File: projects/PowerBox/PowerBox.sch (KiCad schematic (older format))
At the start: 39 parts

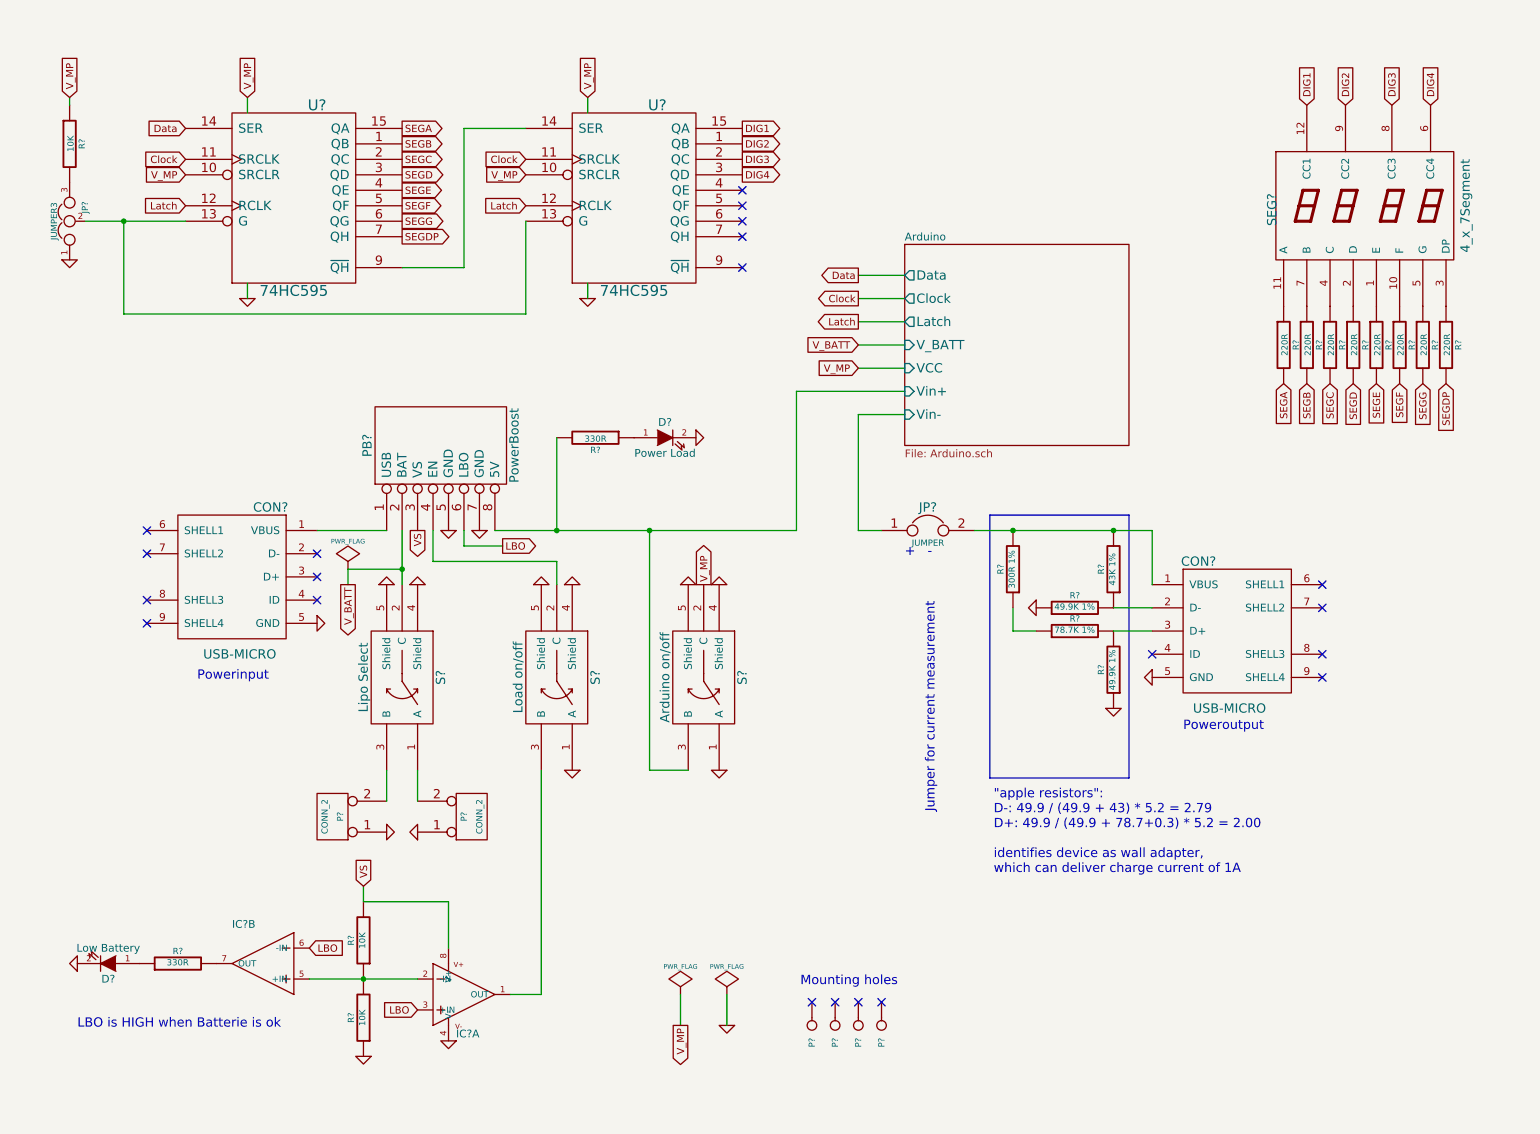
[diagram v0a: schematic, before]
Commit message: erc warnings solved
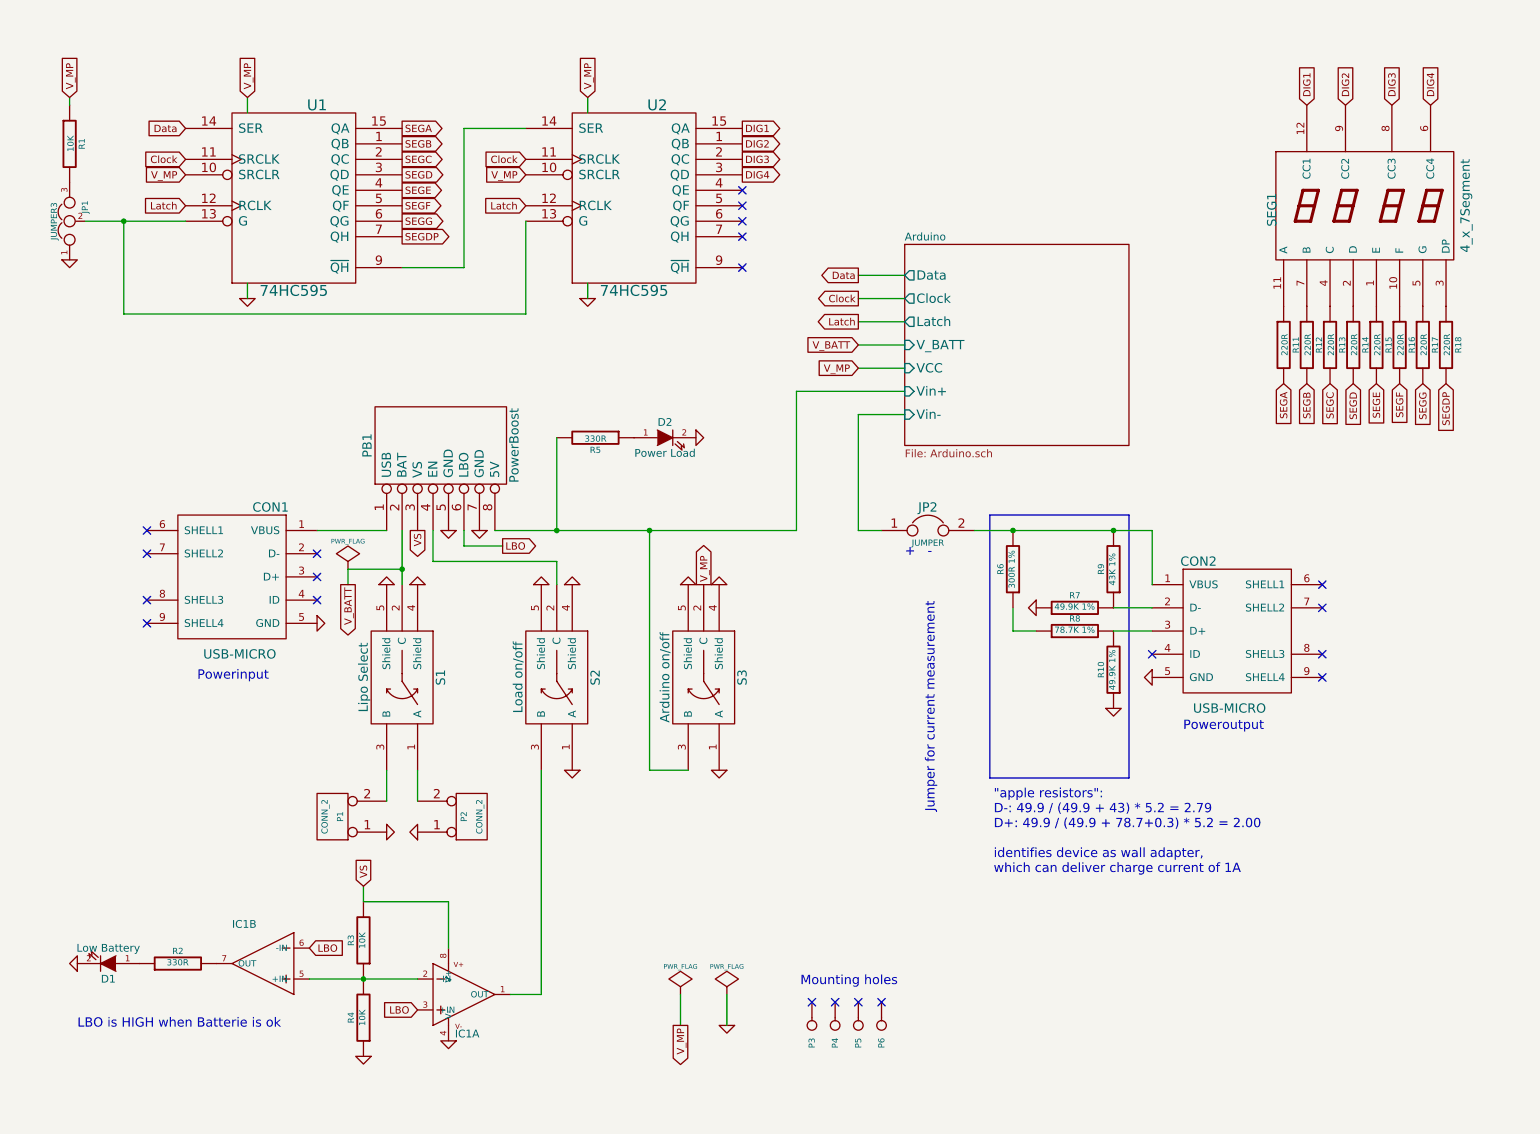
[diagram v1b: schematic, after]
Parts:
- gave numbers to parts that had none: 38

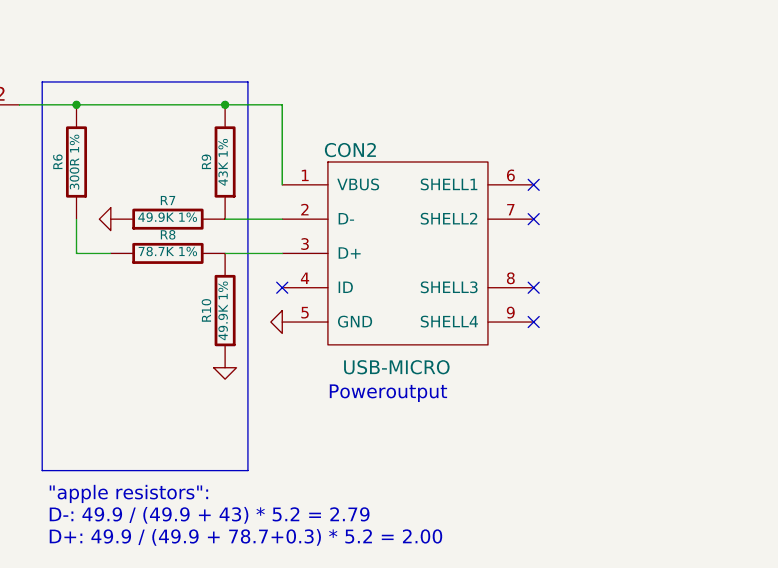
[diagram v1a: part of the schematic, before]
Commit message: more footprints added
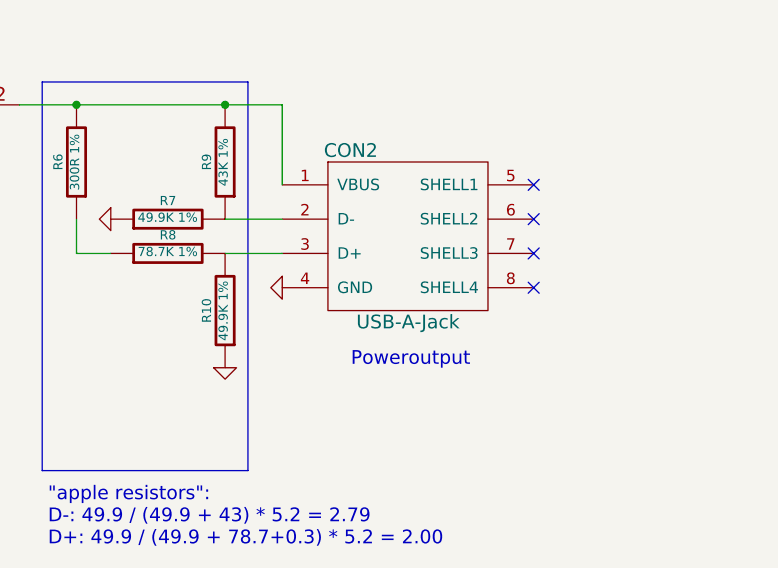
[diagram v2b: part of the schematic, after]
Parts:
- removed CON2: USB-MICRO, symbol USB-MICRO
- added CON2: USB-A-Jack, frep:USB-A-Jack, symbol USB-A-Jack
- CON1: footprint (none) -> frep:USB_Micro
- D1, D2: footprint (none) -> frep:LED-0805
- IC1: footprint SparkFun-SO08 -> frep:SOIC8
- JP1: footprint (none) -> frep:Pin_Proto_Straight_1x03
- JP2: footprint (none) -> frep:Pin_Proto_Straight_1x02
- P1: footprint (none) -> frep:JST-PH-2-THM
- P2: footprint (none) -> frep:JST-PH-2-THM-RA
- P3, P4, P5, P6: footprint (none) -> frep:MountingHole_3mm
- PB1: footprint (none) -> frep:Powerboost1000C
- R1, R10, R11, R12, R13, R14, R15, R16, R17, R18, R2, R3, R4, R5, R6, R7, R8, R9: footprint (none) -> frep:R0805
- S1, S2, S3: footprint (none) -> frep:Switch_SPDT
- SEG1: footprint (none) -> frep:4digit7segment
- U1, U2: footprint (none) -> frep:SO16
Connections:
- net GND: now also CON2.4 (GND)
- net at JP2.2, R6.2, R9.2: now also CON2.1 (VBUS)
- net at R7.2, R9.1: now also CON2.2 (D-)
- net at R10.2, R8.2: now also CON2.3 (D+)
- no-connect marks 21 -> 20
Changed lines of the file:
@@
 LIBS:frep
 LIBS:PowerBox-cache
-EELAYER 24 0
+EELAYER 25 0
 EELAYER END
 $Descr A4 11693 8268
@@
 F 0 "CON1" H 2000 4650 60  0000 C CNN
 F 1 "USB-MICRO" H 2200 3700 60  0000 C CNN
-F 2 "" H 2250 4200 60  0000 C CNN
+F 2 "frep:USB_Micro" H 2250 4200 60  0001 C CNN
 F 3 "" H 2250 4200 60  0000 C CNN
 	1    2250 4200
@@
 F 0 "S1" H 3350 5100 60  0000 C CNN
 F 1 "Lipo Select" H 3350 4600 60  0000 C CNN
-F 2 "" H 3350 4850 60  0000 C CNN
+F 2 "frep:Switch_SPDT" H 3350 4850 60  0001 C CNN
 F 3 "" H 3350 4850 60  0000 C CNN
 	1    3350 4850
@@
 F 0 "P1" V 2850 5750 40  0000 C CNN
 F 1 "CONN_2" V 2950 5750 40  0000 C CNN
-F 2 "" H 2900 5750 60  0000 C CNN
+F 2 "frep:JST-PH-2-THM" H 2900 5750 60  0001 C CNN
 F 3 "" H 2900 5750 60  0000 C CNN
 	1    2900 5750
@@
 F 0 "P2" V 3750 5750 40  0000 C CNN
 F 1 "CONN_2" V 3850 5750 40  0000 C CNN
-F 2 "" H 3800 5750 60  0000 C CNN
+F 2 "frep:JST-PH-2-THM-RA" H 3800 5750 60  0001 C CNN
 F 3 "" H 3800 5750 60  0000 C CNN
 	1    3800 5750
@@
 F 0 "S2" H 4350 5100 60  0000 C CNN
 F 1 "Load on/off" H 4350 4600 60  0000 C CNN
-F 2 "" H 4350 4850 60  0000 C CNN
+F 2 "frep:Switch_SPDT" H 4350 4850 60  0001 C CNN
 F 3 "" H 4350 4850 60  0000 C CNN
 	1    4350 4850
@@
 F 0 "S3" H 5300 5100 60  0000 C CNN
 F 1 "Arduino on/off" H 5300 4600 60  0000 C CNN
-F 2 "" H 5300 4850 60  0000 C CNN
+F 2 "frep:Switch_SPDT" H 5300 4850 60  0001 C CNN
 F 3 "" H 5300 4850 60  0000 C CNN
 	1    5300 4850
@@
 Text GLabel 5300 4250 1    47   Output ~ 0
 V_MP
-$Comp
-L USB-MICRO CON2
-U 1 1 5581E5BD
-P 8750 4550
-F 0 "CON2" H 8500 5000 60  0000 C CNN
-F 1 "USB-MICRO" H 8700 4050 60  0000 C CNN
-F 2 "" H 8750 4550 60  0000 C CNN
-F 3 "" H 8750 4550 60  0000 C CNN
-	1    8750 4550
-	1    0    0    -1
-$EndComp
-Text Notes 8400 5200 0    60   ~ 0
+Text Notes 8500 5050 0    60   ~ 0
 Poweroutput
 $Comp
 L GND #PWR014
 U 1 1 5581E5DC
-P 8200 4850
-F 0 "#PWR014" H 8200 4850 30  0001 C CNN
-F 1 "GND" H 8200 4780 30  0001 C CNN
-F 2 "" H 8200 4850 60  0000 C CNN
-F 3 "" H 8200 4850 60  0000 C CNN
-	1    8200 4850
+P 8200 4700
+F 0 "#PWR014" H 8200 4700 30  0001 C CNN
+F 1 "GND" H 8200 4630 30  0001 C CNN
+F 2 "" H 8200 4700 60  0000 C CNN
+F 3 "" H 8200 4700 60  0000 C CNN
+	1    8200 4700
 	0    1    1    0
 $EndComp
-NoConn ~ 8200 4700
 NoConn ~ 1700 3900
 NoConn ~ 1700 4050
@@
 NoConn ~ 9300 4400
 NoConn ~ 9300 4700
-NoConn ~ 9300 4850
+NoConn ~ 9300 4550
 Wire Wire Line
 	4950 3900 4950 5450
@@
 F 0 "R9" V 8030 4150 40  0000 C CNN
 F 1 "43K 1%" V 7957 4151 40  0000 C CNN
-F 2 "" V 7880 4150 30  0000 C CNN
+F 2 "frep:R0805" V 7880 4150 30  0001 C CNN
 F 3 "" H 7950 4150 30  0000 C CNN
 	1    7950 4150
@@
 F 0 "R8" V 7780 4550 40  0000 C CNN
 F 1 "78.7K 1%" V 7707 4551 40  0000 C CNN
-F 2 "" V 7630 4550 30  0000 C CNN
+F 2 "frep:R0805" V 7630 4550 30  0001 C CNN
 F 3 "" H 7700 4550 30  0000 C CNN
 	1    7700 4550
@@
 F 0 "R10" V 8030 4800 40  0000 C CNN
 F 1 "49.9K 1%" V 7957 4801 40  0000 C CNN
-F 2 "" V 7880 4800 30  0000 C CNN
+F 2 "frep:R0805" V 7880 4800 30  0001 C CNN
 F 3 "" H 7950 4800 30  0000 C CNN
 	1    7950 4800
@@
 F 0 "R7" V 7780 4400 40  0000 C CNN
 F 1 "49.9K 1%" V 7707 4401 40  0000 C CNN
-F 2 "" V 7630 4400 30  0000 C CNN
+F 2 "frep:R0805" V 7630 4400 30  0001 C CNN
 F 3 "" H 7700 4400 30  0000 C CNN
 	1    7700 4400
@@
 F 0 "P6" H 6530 7100 40  0000 L CNN
 F 1 "CONN_1" H 6450 7155 30  0001 C CNN
-F 2 "" H 6450 7100 60  0000 C CNN
+F 2 "frep:MountingHole_3mm" H 6450 7100 60  0001 C CNN
 F 3 "" H 6450 7100 60  0000 C CNN
 	1    6450 7100
@@
 F 0 "P5" H 6380 7100 40  0000 L CNN
 F 1 "CONN_1" H 6300 7155 30  0001 C CNN
-F 2 "" H 6300 7100 60  0000 C CNN
+F 2 "frep:MountingHole_3mm" H 6300 7100 60  0001 C CNN
 F 3 "" H 6300 7100 60  0000 C CNN
 	1    6300 7100
@@
 F 0 "P4" H 6230 7100 40  0000 L CNN
 F 1 "CONN_1" H 6150 7155 30  0001 C CNN
-F 2 "" H 6150 7100 60  0000 C CNN
+F 2 "frep:MountingHole_3mm" H 6150 7100 60  0001 C CNN
 F 3 "" H 6150 7100 60  0000 C CNN
 	1    6150 7100
@@
 F 0 "P3" H 6080 7100 40  0000 L CNN
 F 1 "CONN_1" H 6000 7155 30  0001 C CNN
-F 2 "" H 6000 7100 60  0000 C CNN
+F 2 "frep:MountingHole_3mm" H 6000 7100 60  0001 C CNN
 F 3 "" H 6000 7100 60  0000 C CNN
 	1    6000 7100
@@
 F 0 "IC1" H 3850 6675 50  0000 R TNN
 F 1 "OPAMP-DUALU" H 3850 7100 50  0001 R TNN
-F 2 "SparkFun-SO08" H 3650 7050 50  0001 C CNN
+F 2 "frep:SOIC8" H 3650 7050 50  0001 C CNN
 F 3 "" H 3650 6900 60  0000 C CNN
 	1    3650 6900
@@
 F 0 "IC1" H 2650 6475 50  0000 R TNN
 F 1 "OPAMP-DUALU" H 2650 6900 50  0001 R TNN
-F 2 "SparkFun-SO08" H 2450 6850 50  0001 C CNN
+F 2 "frep:SOIC8" H 2450 6850 50  0001 C CNN
 F 3 "" H 2450 6700 60  0000 C CNN
 	2    2450 6700
@@
 F 0 "R3" V 3180 6550 40  0000 C CNN
 F 1 "10K" V 3107 6551 40  0000 C CNN
-F 2 "" V 3030 6550 30  0000 C CNN
+F 2 "frep:R0805" V 3030 6550 30  0001 C CNN
 F 3 "" H 3100 6550 30  0000 C CNN
 	1    3100 6550
@@
 F 0 "R4" V 3180 7050 40  0000 C CNN
 F 1 "10K" V 3107 7051 40  0000 C CNN
-F 2 "" V 3030 7050 30  0000 C CNN
+F 2 "frep:R0805" V 3030 7050 30  0001 C CNN
 F 3 "" H 3100 7050 30  0000 C CNN
 	1    3100 7050
@@
 F 0 "R2" V 1980 6700 40  0000 C CNN
 F 1 "330R" V 1907 6701 40  0000 C CNN
-F 2 "" V 1830 6700 30  0000 C CNN
+F 2 "frep:R0805" V 1830 6700 30  0001 C CNN
 F 3 "" H 1900 6700 30  0000 C CNN
 	1    1900 6700
@@
 F 0 "D1" H 1450 6800 50  0000 C CNN
 F 1 "Low Battery" H 1450 6600 50  0000 C CNN
-F 2 "" H 1450 6700 60  0000 C CNN
+F 2 "frep:LED-0805" H 1450 6700 60  0001 C CNN
 F 3 "" H 1450 6700 60  0000 C CNN
 	1    1450 6700
@@
 F 0 "R5" V 4680 3300 40  0000 C CNN
 F 1 "330R" V 4607 3301 40  0000 C CNN
-F 2 "" V 4530 3300 30  0000 C CNN
+F 2 "frep:R0805" V 4530 3300 30  0001 C CNN
 F 3 "" H 4600 3300 30  0000 C CNN
 	1    4600 3300
@@
 F 0 "D2" H 5050 3400 50  0000 C CNN
 F 1 "Power Load" H 5050 3200 50  0000 C CNN
-F 2 "" H 5050 3300 60  0000 C CNN
+F 2 "frep:LED-0805" H 5050 3300 60  0001 C CNN
 F 3 "" H 5050 3300 60  0000 C CNN
 	1    5050 3300
@@
 F 0 "PB1" H 3600 3825 60  0000 C CNN
 F 1 "PowerBoost" H 3600 2875 60  0000 C CNN
-F 2 "" H 3600 3250 60  0000 C CNN
+F 2 "frep:Powerboost1000C" H 3600 3250 60  0001 C CNN
 F 3 "" H 3600 3250 60  0000 C CNN
 	1    3600 3350
@@
 F 0 "R6" V 7380 4150 40  0000 C CNN
 F 1 "300R 1%" V 7307 4151 40  0000 C CNN
-F 2 "" V 7230 4150 30  0000 C CNN
+F 2 "frep:R0805" V 7230 4150 30  0001 C CNN
 F 3 "" H 7300 4150 30  0000 C CNN
 	1    7300 4150
@@
 F 0 "JP2" H 6750 4050 60  0000 C CNN
 F 1 "JUMPER" H 6750 3820 40  0000 C CNN
-F 2 "" H 6750 3900 60  0000 C CNN
+F 2 "frep:Pin_Proto_Straight_1x02" H 6750 3900 60  0001 C CNN
 F 3 "" H 6750 3900 60  0000 C CNN
 	1    6750 3900
@@
 F 0 "SEG1" V 8975 1775 60  0000 C CNN
 F 1 "4_x_7Segment" V 10225 1800 60  0000 C CNN
-F 2 "" H 9500 1800 60  0000 C CNN
+F 2 "frep:4digit7segment" H 9500 1800 60  0001 C CNN
 F 3 "" H 9500 1800 60  0000 C CNN
 	1    9600 1800
@@
 F 0 "U1" H 2800 2350 70  0000 C CNN
 F 1 "74HC595" H 2650 1150 70  0000 C CNN
-F 2 "" H 2650 1750 60  0000 C CNN
+F 2 "frep:SO16" H 2650 1750 60  0001 C CNN
 F 3 "" H 2650 1750 60  0000 C CNN
 	1    2650 1750
@@
 F 0 "U2" H 5000 2350 70  0000 C CNN
 F 1 "74HC595" H 4850 1150 70  0000 C CNN
-F 2 "" H 4850 1750 60  0000 C CNN
+F 2 "frep:SO16" H 4850 1750 60  0001 C CNN
 F 3 "" H 4850 1750 60  0000 C CNN
 	1    4850 1750
@@
 F 0 "R1" V 1280 1400 40  0000 C CNN
 F 1 "10K" V 1207 1401 40  0000 C CNN
-F 2 "" V 1130 1400 30  0000 C CNN
+F 2 "frep:R0805" V 1130 1400 30  0001 C CNN
 F 3 "" H 1200 1400 30  0000 C CNN
 	1    1200 1400
@@
 F 0 "JP1" H 1250 1800 40  0000 L CNN
 F 1 "JUMPER3" H 1200 2000 40  0000 C CNN
-F 2 "" H 1200 1900 60  0000 C CNN
+F 2 "frep:Pin_Proto_Straight_1x03" H 1200 1900 60  0001 C CNN
 F 3 "" H 1200 1900 60  0000 C CNN
 	1    1200 1900
@@
 F 0 "R11" V 9130 2700 40  0000 C CNN
 F 1 "220R" V 9057 2701 40  0000 C CNN
-F 2 "" V 8980 2700 30  0000 C CNN
+F 2 "frep:R0805" V 8980 2700 30  0001 C CNN
 F 3 "" H 9050 2700 30  0000 C CNN
 	1    9050 2700
@@
 F 0 "R12" V 9280 2700 40  0000 C CNN
 F 1 "220R" V 9207 2701 40  0000 C CNN
-F 2 "" V 9130 2700 30  0000 C CNN
+F 2 "frep:R0805" V 9130 2700 30  0001 C CNN
 F 3 "" H 9200 2700 30  0000 C CNN
 	1    9200 2700
@@
 F 0 "R13" V 9430 2700 40  0000 C CNN
 F 1 "220R" V 9357 2701 40  0000 C CNN
-F 2 "" V 9280 2700 30  0000 C CNN
+F 2 "frep:R0805" V 9280 2700 30  0001 C CNN
 F 3 "" H 9350 2700 30  0000 C CNN
 	1    9350 2700
@@
 F 0 "R14" V 9580 2700 40  0000 C CNN
 F 1 "220R" V 9507 2701 40  0000 C CNN
-F 2 "" V 9430 2700 30  0000 C CNN
+F 2 "frep:R0805" V 9430 2700 30  0001 C CNN
 F 3 "" H 9500 2700 30  0000 C CNN
 	1    9500 2700
@@
 F 0 "R15" V 9730 2700 40  0000 C CNN
 F 1 "220R" V 9657 2701 40  0000 C CNN
-F 2 "" V 9580 2700 30  0000 C CNN
+F 2 "frep:R0805" V 9580 2700 30  0001 C CNN
 F 3 "" H 9650 2700 30  0000 C CNN
 	1    9650 2700
@@
 F 0 "R16" V 9880 2700 40  0000 C CNN
 F 1 "220R" V 9807 2701 40  0000 C CNN
-F 2 "" V 9730 2700 30  0000 C CNN
+F 2 "frep:R0805" V 9730 2700 30  0001 C CNN
 F 3 "" H 9800 2700 30  0000 C CNN
 	1    9800 2700
@@
 F 0 "R17" V 10030 2700 40  0000 C CNN
 F 1 "220R" V 9957 2701 40  0000 C CNN
-F 2 "" V 9880 2700 30  0000 C CNN
+F 2 "frep:R0805" V 9880 2700 30  0001 C CNN
 F 3 "" H 9950 2700 30  0000 C CNN
 	1    9950 2700
@@
 F 0 "R18" V 10180 2700 40  0000 C CNN
 F 1 "220R" V 10107 2701 40  0000 C CNN
-F 2 "" V 10030 2700 30  0000 C CNN
+F 2 "frep:R0805" V 10030 2700 30  0001 C CNN
 F 3 "" H 10100 2700 30  0000 C CNN
 	1    10100 2700
 	1    0    0    -1
 $EndComp
+$Comp
+L USB-A-Jack CON2
+U 1 1 558F1B9A
+P 8750 4550
+F 0 "CON2" H 8500 5000 60  0000 C CNN
+F 1 "USB-A-Jack" H 8750 4250 60  0000 C CNN
+F 2 "frep:USB-A-Jack" H 8750 4550 60  0001 C CNN
+F 3 "" H 8750 4550 60  0000 C CNN
+	1    8750 4550
+	1    0    0    -1
+$EndComp
